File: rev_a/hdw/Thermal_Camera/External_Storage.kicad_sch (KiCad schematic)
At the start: 43 parts

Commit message: added some more USB stuff
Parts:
- added J?: SPI FLASH, symbol Connector_Generic:Conn_01x05
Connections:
- net FLASH_SPI_MISO: now also J?.4 (Pin_4)
- net FLASH_SPI_MOSI: now also J?.3 (Pin_3)
- net FLASH_SPI_SCK: now also J?.2 (Pin_2)
- net GND: now also J?.5 (Pin_5)
- net ~{FLASH_SPI_CS}: now also J?.1 (Pin_1)
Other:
- note added: "SD CARD, SPI FLASH BREAK OUT A SPI TO SD CARD AS INSURANCE"
- note removed: "SD CARD, SPI FLASH BREAK OUT A SPI TO SD CARD AS INSURANCE BREAK OUT FLASH SPI TO A HEADER FOR PROGRAMMING"
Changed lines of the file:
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@@
     (stroke (width 0) (type default))
   )
+  (wire (pts (xy 237.49 154.94) (xy 237.49 152.4))
+    (stroke (width 0) (type default))
+  )
   (wire (pts (xy 87.63 39.37) (xy 87.63 60.96))
     (stroke (width 0) (type default))
@@
     (stroke (width 0) (type default))
   )
+  (wire (pts (xy 237.49 152.4) (xy 240.03 152.4))
+    (stroke (width 0) (type default))
+  )
   (wire (pts (xy 92.71 91.44) (xy 95.25 91.44))
     (stroke (width 0) (type default))
@@
     (stroke (width 0) (type default))
   )
-  (text "SD CARD, SPI FLASH\nBREAK OUT A SPI TO SD CARD AS INSURANCE\nBREAK OUT FLASH SPI TO A HEADER FOR PROGRAMMING"
+  (text "SD CARD, SPI FLASH\nBREAK OUT A SPI TO SD CARD AS INSURANCE"
     (at 10.16 189.865 0)
     (effects (font (face "Courier New") (size 5.08 5.08) (thickness 1.016) bold (color 194 0 0 1)) (justify left bottom))
@@
     )
   )
+  (global_label "FLASH_SPI_SCK" (shape passive) (at 240.03 144.78 180) (fields_autoplaced)
+    (effects (font (size 1.27 1.27)) (justify right))
+    (property "Intersheetrefs" "${INTERSHEET_REFS}" (at 223.7212 144.78 0)
+      (effects (font (size 1.27 1.27)) (justify right) hide)
+    )
+  )
   (global_label "~{FLASH_SPI_CS}" (shape input) (at 71.12 139.7 180) (fields_autoplaced)
     (effects (font (size 1.27 1.27)) (justify right))
@@
     )
   )
+  (global_label "FLASH_SPI_MOSI" (shape passive) (at 240.03 147.32 180) (fields_autoplaced)
+    (effects (font (size 1.27 1.27)) (justify right))
+    (property "Intersheetrefs" "${INTERSHEET_REFS}" (at 222.8745 147.32 0)
+      (effects (font (size 1.27 1.27)) (justify right) hide)
+    )
+  )
   (global_label "SDHC_SDCK" (shape bidirectional) (at 71.12 53.34 180) (fields_autoplaced)
     (effects (font (size 1.27 1.27)) (justify right))
@@
     )
   )
+  (global_label "~{FLASH_SPI_CS}" (shape passive) (at 240.03 142.24 180) (fields_autoplaced)
+    (effects (font (size 1.27 1.27)) (justify right))
+    (property "Intersheetrefs" "${INTERSHEET_REFS}" (at 224.9912 142.24 0)
+      (effects (font (size 1.27 1.27)) (justify right) hide)
+    )
+  )
   (global_label "SD_PWR_EN" (shape input) (at 92.71 91.44 180) (fields_autoplaced)
     (effects (font (size 1.27 1.27)) (justify right))
@@
     )
   )
+  (global_label "FLASH_SPI_MISO" (shape passive) (at 240.03 149.86 180) (fields_autoplaced)
+    (effects (font (size 1.27 1.27)) (justify right))
+    (property "Intersheetrefs" "${INTERSHEET_REFS}" (at 222.8745 149.86 0)
+      (effects (font (size 1.27 1.27)) (justify right) hide)
+    )
+  )
   (global_label "~{FLASH_SPI_WP}" (shape input) (at 71.12 149.86 180) (fields_autoplaced)
     (effects (font (size 1.27 1.27)) (justify right))
@@
     )
   )
+  (symbol (lib_id "Connector_Generic:Conn_01x05") (at 245.11 147.32 0) (unit 1)
+    (in_bom yes) (on_board yes) (dnp no)
+    (property "Reference" "J?" (at 245.11 139.7 0)
+      (effects (font (size 1.27 1.27)))
+    )
+    (property "Value" "SPI FLASH" (at 245.11 154.94 0)
+      (effects (font (size 1.27 1.27)))
+    )
+    (property "Footprint" "" (at 245.11 147.32 0)
+      (effects (font (size 1.27 1.27)) hide)
+    )
+    (property "Datasheet" "~" (at 245.11 147.32 0)
+      (effects (font (size 1.27 1.27)) hide)
+    )
+    (pin "1")
+    (pin "2")
+    (pin "3")
+    (pin "4")
+    (pin "5")
+    (instances
+      (project "Thermal_Camera"
+        (path "/4bd21e0b-5408-4b93-866e-c82ac5b31fa9/21507370-f247-4205-8e94-91a7207a6f8b"
+          (reference "J?") (unit 1)
+        )
+      )
+    )
+  )
   (symbol (lib_id "power:GND") (at 107.95 104.14 0) (mirror y) (unit 1)
     (in_bom yes) (on_board yes) (dnp no)
@@
         )
       )
+    )
+  )
+  (symbol (lib_id "power:GND") (at 237.49 154.94 0) (unit 1)
+    (in_bom yes) (on_board yes) (dnp no)
+    (property "Reference" "#PWR0190" (at 237.49 161.29 0)
+      (effects (font (size 1.27 1.27)) hide)
+    )
+    (property "Value" "GND" (at 237.49 158.75 0)
+      (effects (font (size 1.27 1.27)))
+    )
+    (property "Footprint" "" (at 237.49 154.94 0)
+      (effects (font (size 1.27 1.27)) hide)
+    )
+    (property "Datasheet" "" (at 237.49 154.94 0)
+      (effects (font (size 1.27 1.27)) hide)
+    )
+    (pin "1")
+    (instances
+      (project "Thermal_Camera"
+        (path "/4bd21e0b-5408-4b93-866e-c82ac5b31fa9/21507370-f247-4205-8e94-91a7207a6f8b"
+          (reference "#PWR0190") (unit 1)
+        )
+      )

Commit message: lots of random schematic progress
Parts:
- removed J?: SPI FLASH, symbol Connector_Generic:Conn_01x05
- added R? (x4): 10, Resistors_SMD:R_0603, symbol Custom_Library:R_Custom
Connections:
- net SDHC_SDCK: no longer D?.6 (K4), R1501.2
- net SDHC_SDCMD: no longer D?.3 (K2), R1501.2
- net SDHC_SDDATA0: no longer D?.4 (K3), R1501.2
- net SDHC_SDDATA1: no longer D?.1 (K1), R1501.2
- net SDHC_SDDATA2: no longer D?.4 (K3), R1501.2
- net SDHC_SDDATA3: no longer D?.1 (K1), R1501.2
- net ~{FLASH_SPI_CS}: now also R?.2
- net at J?.1 (DAT2), R?.1: now also D?.4 (K3), R1501.2
- net at J?.2 (DAT3/CD), R?.1: now also D?.1 (K1), R1501.2, R?.1
- net at J?.3 (CMD), R?.1: now also D?.3 (K2), R1501.2, R?.1
- net at J?.5 (CLK), R?.1: now also D?.6 (K4), R1501.2, R?.1
- net at J?.7 (DAT0), R?.1: now also D?.4 (K3), R1501.2, R?.1
- net at J?.8 (DAT1), R?.1: now also D?.1 (K1), R1501.2
- new net SD_SPI_MISO: R?.2
- new net SD_SPI_MOSI: R?.2
- new net SD_SPI_SCK: R?.2
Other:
- note removed: "SD CARD, SPI FLASH BREAK OUT A SPI TO SD CARD AS INSURANCE"
- moved on the sheet: C?, D?A, D?B, D?C, D?D, J?, R1501, R?, U?

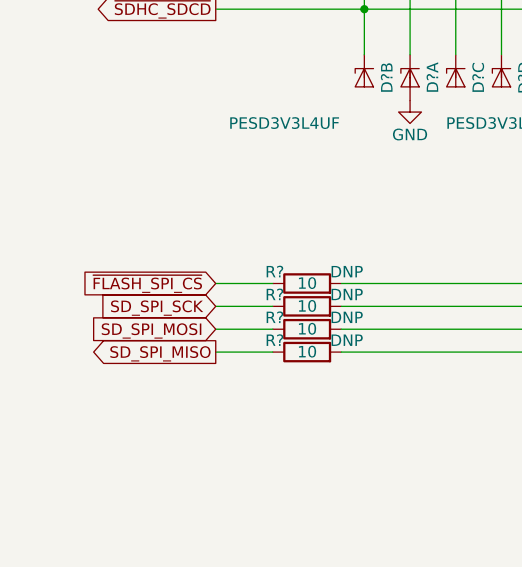
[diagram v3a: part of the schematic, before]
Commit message: assigned some GPIO pins
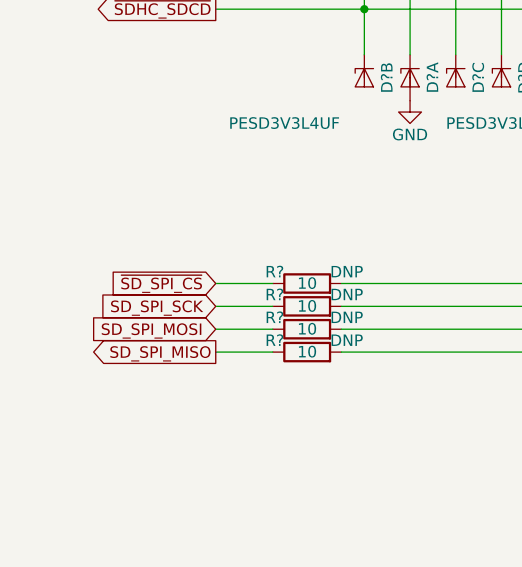
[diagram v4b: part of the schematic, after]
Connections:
- net ~{FLASH_SPI_CS}: no longer R?.2
- new net ~{SD_SPI_CS}: R?.2
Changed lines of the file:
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@@
     )
   )
-  (global_label "~{FLASH_SPI_CS}" (shape input) (at 35.56 93.98 180) (fields_autoplaced)
+  (global_label "~{SD_SPI_CS}" (shape input) (at 35.56 93.98 180) (fields_autoplaced)
     (effects (font (size 1.27 1.27)) (justify right))
-    (property "Intersheetrefs" "${INTERSHEET_REFS}" (at 19.3305 93.98 0)
+    (property "Intersheetrefs" "${INTERSHEET_REFS}" (at 22.6757 93.98 0)
       (effects (font (size 1.27 1.27)) (justify right) hide)
     )

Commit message: lots of schematic progress
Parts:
- added R2011: 10k, symbol Custom_Library:R_Custom
- C? (x4): footprint Capacitors_SMD:C_0603 -> (none); Digi-Key PN 1276-1871-1-ND -> (none); display_footprint 0603 -> (none)
- C? (x3): footprint Capacitors_SMD:C_0603 -> (none); Digi-Key PN 1276-1935-1-ND -> (none); display_footprint 0603 -> (none)
- R2001, R2002, R2003, R2004, R2005, R2006, R2025, R2026, R2027, R2028, R2030: renamed from R?; footprint Resistors_SMD:R_0603 -> (none); Digi-Key PN 541-2982-1-ND -> (none); Wattage 1/10W -> (none); display_footprint 0603 -> (none)
- R2007, R2008, R2009, R2010: renamed from R?; footprint Resistors_SMD:R_0603 -> (none); Digi-Key PN 541-2982-1-ND -> (none); Wattage 1/10W -> (none); display_footprint 0603 -> (none); now not fitted
- R? (x14): renamed from R1501; footprint Resistors_SMD:R_0603 -> (none); Digi-Key PN 541-10.0KHCT-ND -> (none); Wattage 1/10W -> (none); display_footprint 0603 -> (none)
- gave numbers to parts that had none: 5
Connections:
- net +3.0V_SD: now also R2011.1
- net ~{SDHC_SDWP}: now also R2011.2
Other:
- note removed: "?"

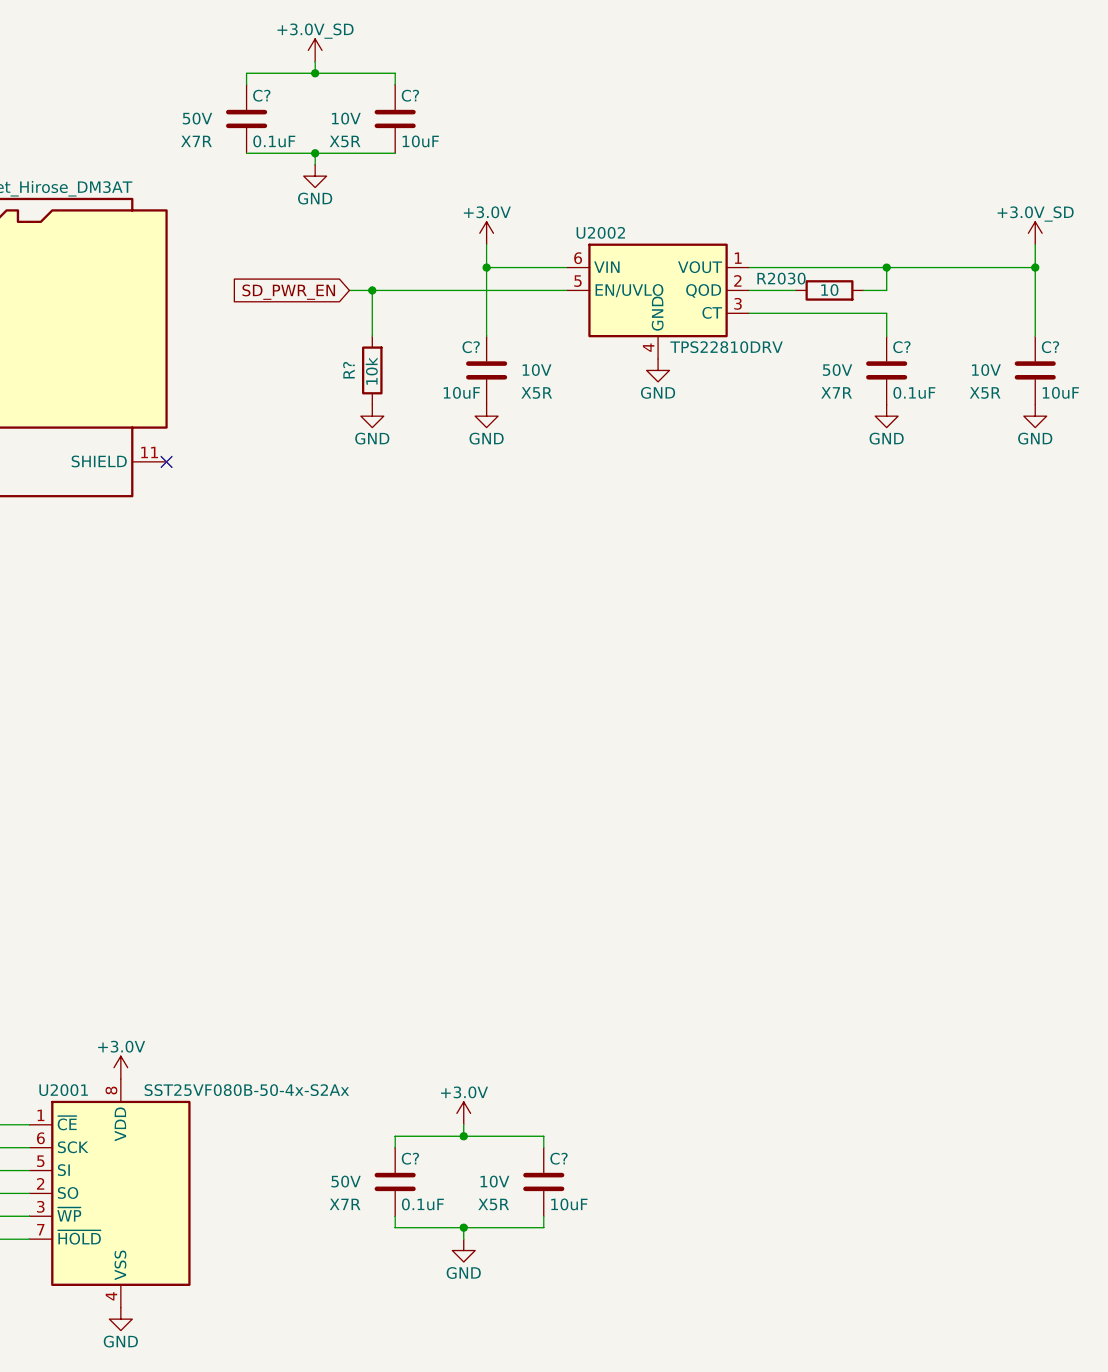
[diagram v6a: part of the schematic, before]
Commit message: assigned a ton of footprints
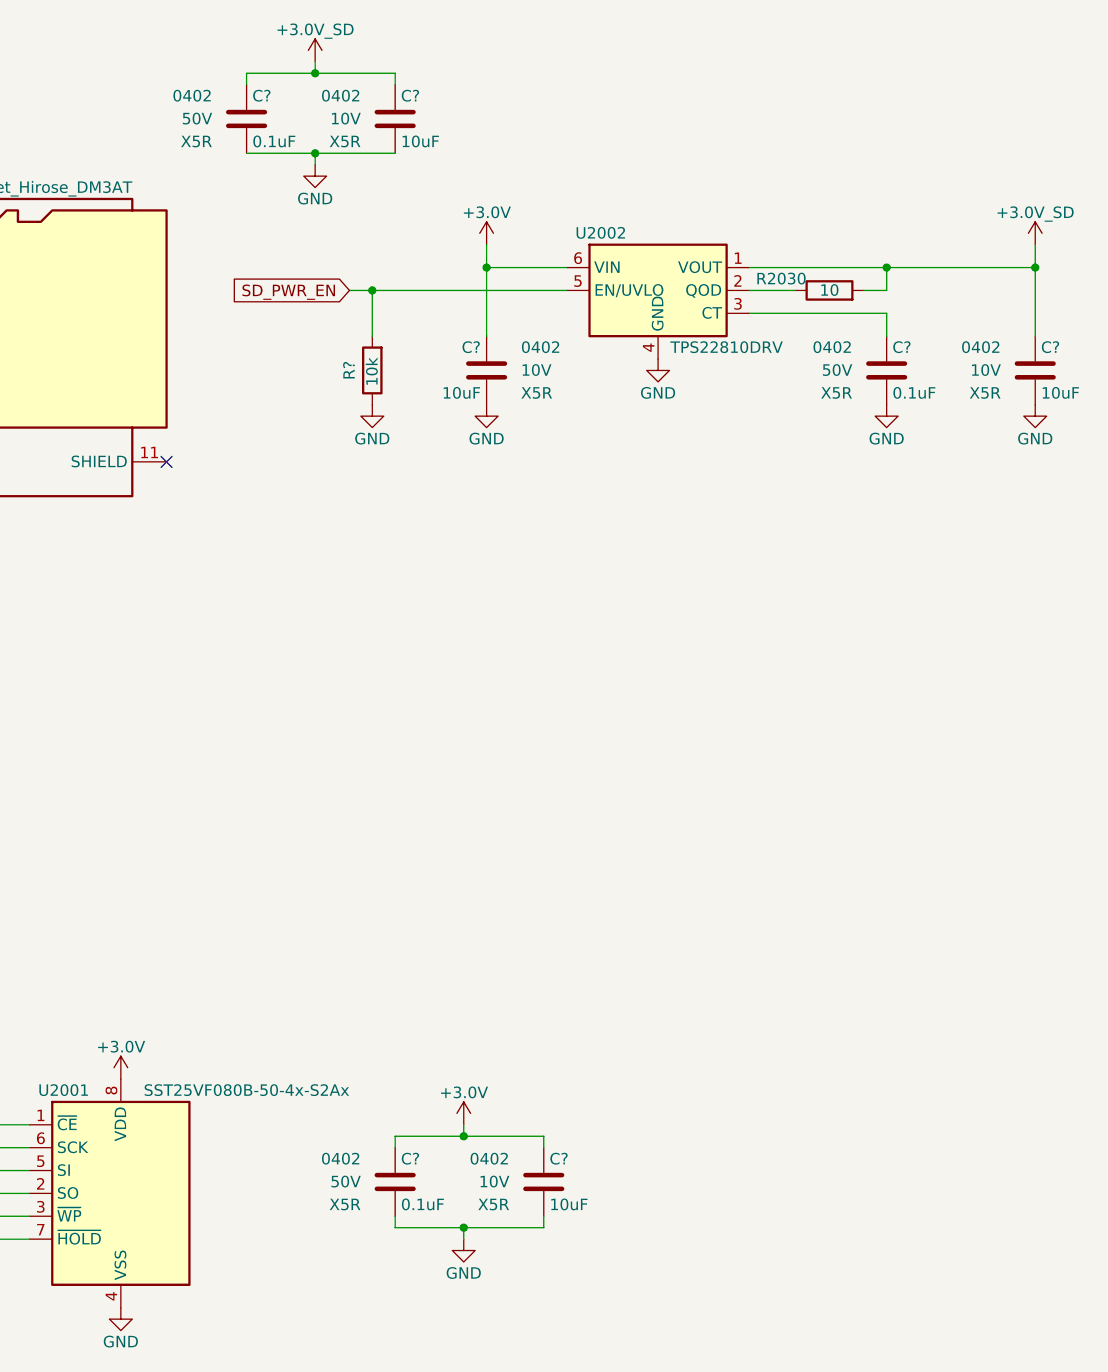
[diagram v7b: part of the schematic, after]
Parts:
- C? (x4): footprint (none) -> Capacitors_SMD:C_0402; display_footprint (none) -> 0402
- C? (x3): footprint (none) -> Capacitors_SMD:C_0402; Dielectric X7R -> X5R; display_footprint (none) -> 0402
- R2001, R2002, R2003, R2004, R2005, R2006, R2007, R2008, R2009, R2010, R2011, R2025, R2026, R2027, R2028, R2030, R? (x14): footprint (none) -> Resistors_SMD:R_0402; Wattage (none) -> 1/16W; display_footprint (none) -> 0402
- U2001: Digi-Key PN (none) -> SST25VF080B-50-4C-S2AF-ND
- U2002: Digi-Key PN (none) -> 296-47868-1-ND

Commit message: assigned some part numbers
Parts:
- C? (x4): Digi-Key PN (none) -> 490-GRM155R61A106ME11DCT-ND
- C? (x3): Digi-Key PN (none) -> 490-10697-1-ND
- J2001: Digi-Key PN (none) -> HR1964CT-ND
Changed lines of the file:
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@@
 			)
 		)
+		(property "Digi-Key PN" "HR1964CT-ND"
+			(at 137.16 53.34 0)
+			(effects
+				(font
+					(size 1.27 1.27)
+				)
+				(hide yes)
+			)
+		)
 		(pin "1"
 		)
@@
 			)
 		)
-		(property "Digi-Key PN" ""
+		(property "Digi-Key PN" "490-GRM155R61A106ME11DCT-ND"
 			(at 199.39 146.05 0)
 			(effects
@@
 			)
 		)
-		(property "Digi-Key PN" ""
+		(property "Digi-Key PN" "490-10697-1-ND"
 			(at 138.176 230.632 0)
 			(effects
@@
 			)
 		)
-		(property "Digi-Key PN" ""
+		(property "Digi-Key PN" "490-GRM155R61A106ME11DCT-ND"
 			(at 182.88 27.94 0)
 			(effects
@@
 			)
 		)
-		(property "Digi-Key PN" ""
+		(property "Digi-Key PN" "490-10697-1-ND"
 			(at 67.056 202.692 0)
 			(effects
@@
 			)
 		)
-		(property "Digi-Key PN" ""
+		(property "Digi-Key PN" "490-10697-1-ND"
 			(at 83.566 320.802 0)
 			(effects
@@
 			)
 		)
-		(property "Digi-Key PN" ""
+		(property "Digi-Key PN" "490-GRM155R61A106ME11DCT-ND"
 			(at 254 55.88 0)
 			(effects
@@
 			)
 		)
-		(property "Digi-Key PN" ""
+		(property "Digi-Key PN" "490-GRM155R61A106ME11DCT-ND"
 			(at 193.04 55.88 0)
 			(effects
